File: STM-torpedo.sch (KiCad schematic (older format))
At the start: 8 parts

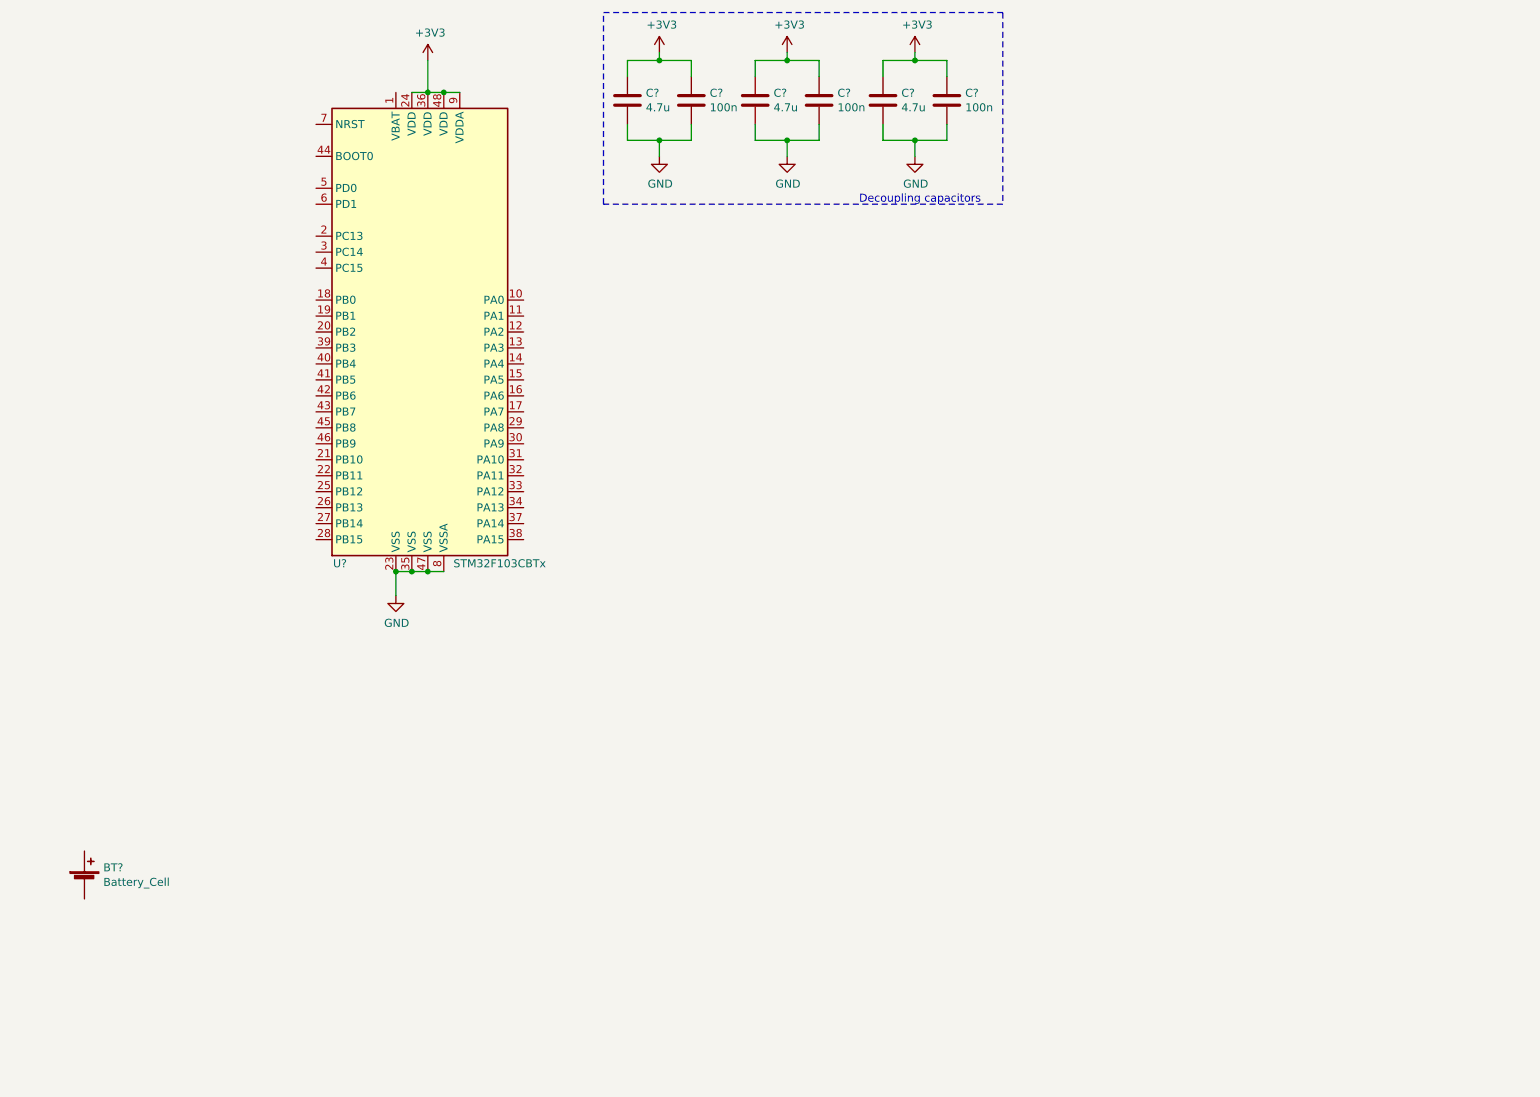
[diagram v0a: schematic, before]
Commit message: Added SWD port to schematic Added power logic (BOOST & LDO) to schematic Added gitignore records for unnecessary kicad files
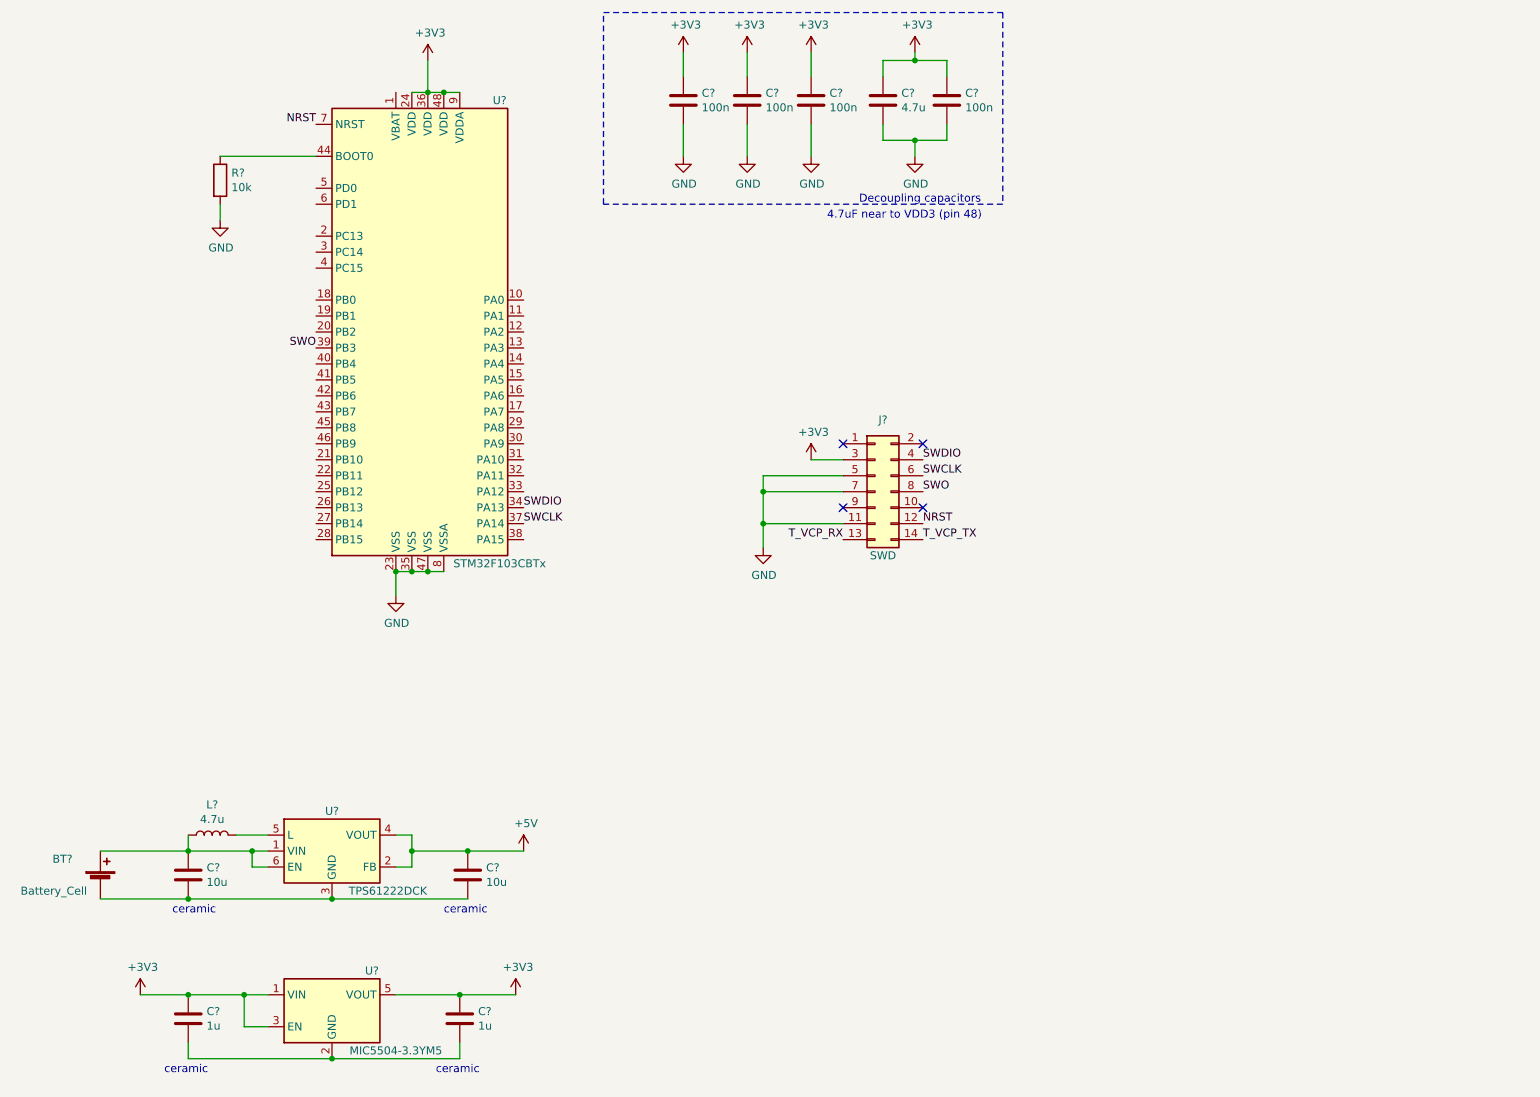
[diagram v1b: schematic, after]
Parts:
- removed C? (x2): 4.7u, symbol Device:C
- removed C?: 100n, symbol Device:C
- added C? (x2): 100n, symbol Device:C
- added C? (x2): 10u, symbol Device:C
- added C? (x2): 1u, symbol Device:C
- added J?: SWD, symbol Connector_Generic:Conn_02x07_Odd_Even
- added L?: 4.7u, symbol Device:L
- added R?: 10k, symbol Device:R
- added U?: TPS61222DCK, Package_TO_SOT_SMD:Texas_R-PDSO-G6, symbol Regulator_Switching:TPS61222DCK
- added U?: MIC5504-3.3YM5, Package_TO_SOT_SMD:SOT-23-5, symbol Regulator_Linear:MIC5504-3.3YM5
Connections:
- net +3V3: now also C?.1, C?.1, C?.1, C?.1, J?.3 (Pin_3), U?.1 (VIN), U?.3 (EN), U?.5 (VOUT)
- net GND: now also C?.2, C?.2, J?.11 (Pin_11), J?.5 (Pin_5), J?.7 (Pin_7), R?.2
- net SWDIO: now reaches U?.34 (PA13)
- net SWDIO: now also J?.4 (Pin_4)
- net SWCLK: now reaches U?.37 (PA14)
- net SWCLK: now also J?.6 (Pin_6)
- net SWO: now reaches U?.39 (PB3)
- net SWO: now also J?.8 (Pin_8)
- net at U?.44 (BOOT0): now also R?.1
- net NRST: now reaches U?.7 (NRST)
- net NRST: now also J?.12 (Pin_12)
- net at BT?.1 (+): now also C?.1, L?.1, U?.1 (VIN), U?.6 (EN)
- net at BT?.2 (-): now also C?.2, C?.2, U?.3 (GND)
- new net: L?.2, U?.5 (L)
- new net: C?.2, C?.2, U?.2 (GND)
- new net +5V: C?.1, U?.2 (FB), U?.4 (VOUT)
- new net T_VCP_RX: J?.13 (Pin_13)
- new net T_VCP_TX: J?.14 (Pin_14)
- no-connect marks 0 -> 4
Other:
- note added: "4.7uF near to VDD3 (pin 48)"
- note added: "ceramic"
- moved on the sheet: BT?, C?

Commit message: Added switches to schematic, and labeled existing components
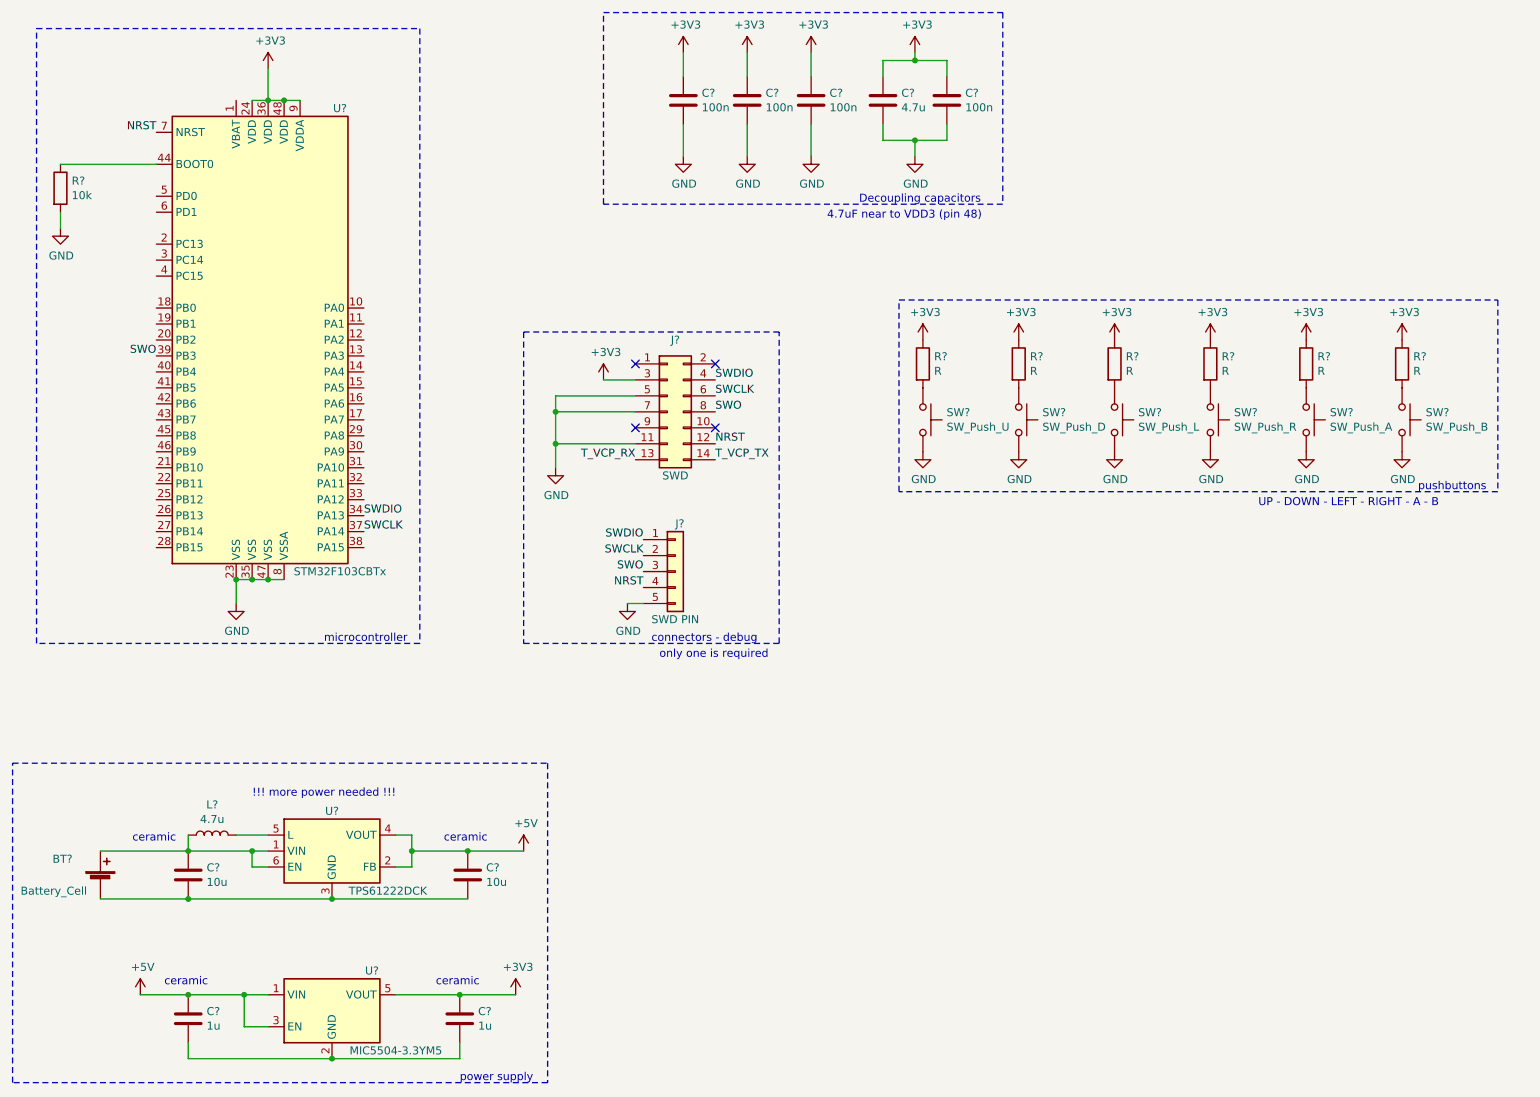
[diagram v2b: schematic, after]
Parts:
- added J?: SWD PIN, symbol Connector_Generic:Conn_01x05
- added R? (x6): R, symbol Device:R
- added SW?: SW_Push_U, symbol Switch:SW_Push
- added SW?: SW_Push_D, symbol Switch:SW_Push
- added SW?: SW_Push_L, symbol Switch:SW_Push
- added SW?: SW_Push_R, symbol Switch:SW_Push
- added SW?: SW_Push_A, symbol Switch:SW_Push
- added SW?: SW_Push_B, symbol Switch:SW_Push
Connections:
- net +3V3: now also R?.1, R?.1, R?.1, R?.1, R?.1, R?.1; no longer C?.1, U?.1 (VIN), U?.3 (EN)
- net +5V: now also C?.1, U?.1 (VIN), U?.3 (EN)
- net GND: now also J?.5 (Pin_5), SW?.2, SW?.2, SW?.2, SW?.2, SW?.2, SW?.2
- net NRST: now also J?.4 (Pin_4)
- net SWCLK: now also J?.2 (Pin_2)
- net SWDIO: now also J?.1 (Pin_1)
- net SWO: now also J?.3 (Pin_3)
- new net: R?.2, SW?.1 (x6)
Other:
- note added: "!!! more power needed !!!\n\n"
- note added: "UP - DOWN - LEFT - RIGHT - A - B"
- note added: "connectors - debug\n"
- note added: "microcontroller\n"
- note added: "only one is required\n"
- note added: "power supply\n"
- note added: "pushbuttons\n"
- moved on the sheet: J?, R?, U?
